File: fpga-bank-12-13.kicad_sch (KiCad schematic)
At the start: 5 parts, among them U1 XC7K410T-2FFG900I

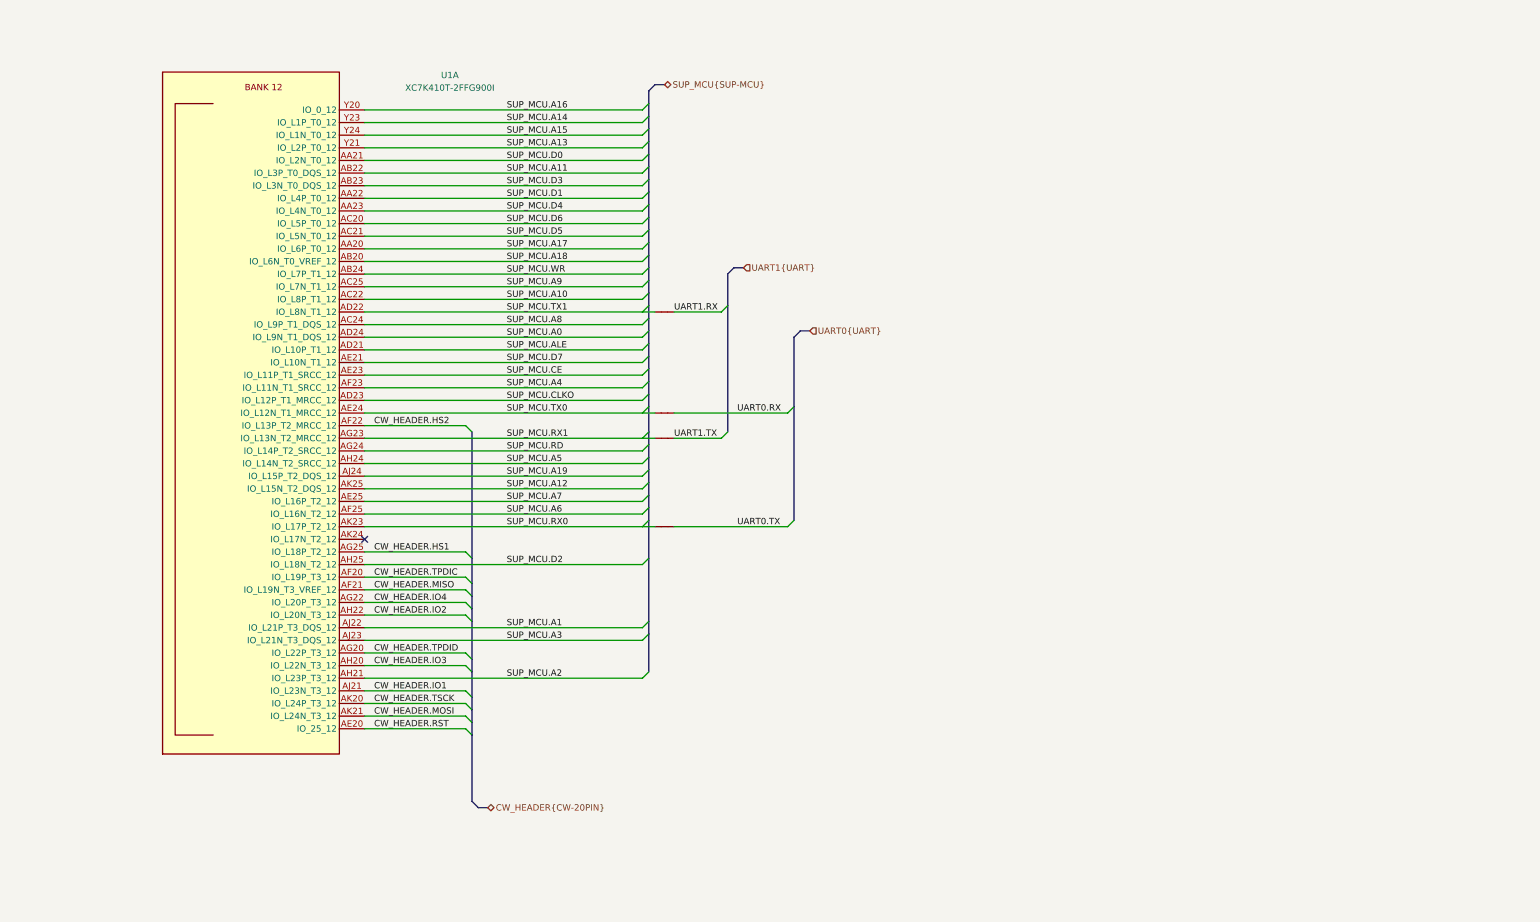
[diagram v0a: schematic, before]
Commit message: [#55729] Switch FPGA symbol to antmicroFPGAChips lib
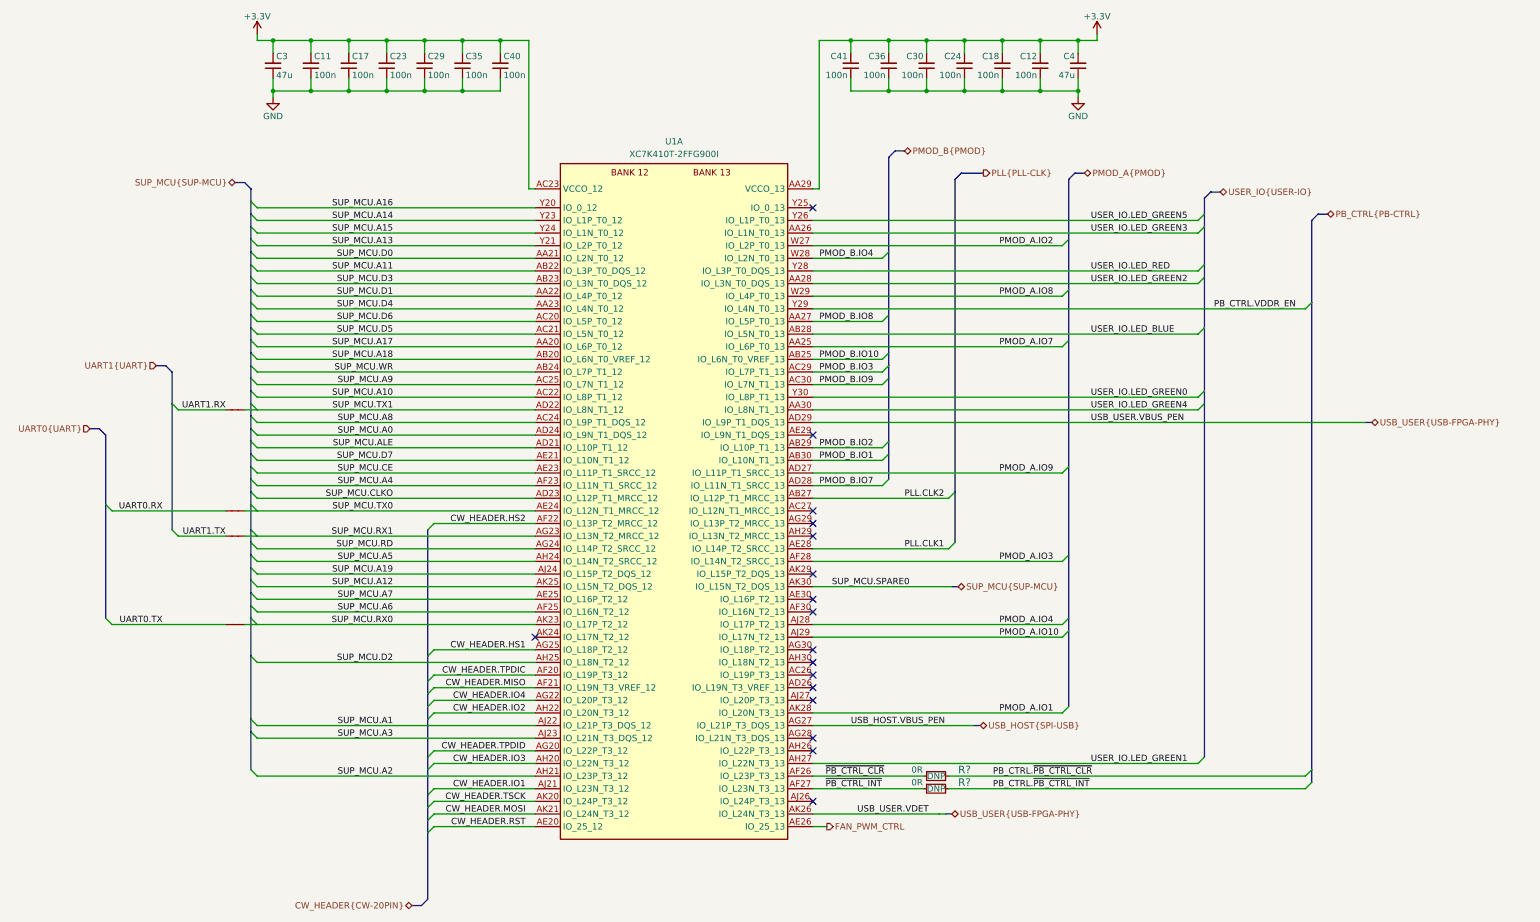
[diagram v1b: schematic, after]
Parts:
- added C11, C12, C17, C18, C23, C24, C29, C30, C35, C36, C40, C41: C_100n_0402, antmicro-footprints:C_0402_1005Metric, symbol antmicroCapacitors0402:C_100n_0402
- added C3, C4: C_47u_0603, antmicro-footprints:C_0603_1608Metric, symbol antmicroCapacitors0603:C_47u_0603
- added R? (x2): R_0R_0402, antmicro-footprints:R_0402_1005Metric, symbol antmicroResistors0402:R_0R_0402
- U1: footprint K410T-devboard-footprints:xc7k410t-2ffg900I -> antmicro-footprints:BGA-900_31x31mm_Layout30x30_P1x1mm_FFG900; symbol K410T-devboard:XC7K410T-2FFG900I -> antmicroFPGAChips:XC7K410T-2FFG900I
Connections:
- new net +3V3: C11.2, C12.2, C17.2, C18.2, C23.2, C24.2, C29.2, C3.2, C30.2, C35.2, C36.2, C4.2, C40.2, C41.2, U1.AA29 (VCCO_13), U1.AB26 (VCCO_13), U1.AC23 (VCCO_12), U1.AD20 (VCCO_12), U1.AD30 (VCCO_13), U1.AE27 (VCCO_13), U1.AF24 (VCCO_12), U1.AG21 (VCCO_12), U1.AH28 (VCCO_13), U1.AJ25 (VCCO_13), U1.AK22 (VCCO_12), U1.Y22 (VCCO_12)
- new net FAN_PWM_CTRL: U1.AE26 (IO_25_13)
- new net GND: C11.1, C12.1, C17.1, C18.1, C23.1, C24.1, C29.1, C3.1, C30.1, C35.1, C36.1, C4.1, C40.1, C41.1
- new net PB_CTRL.VDDR_EN: U1.Y29 (IO_L4N_T0_13)
- new net PB_CTRL.~{PB_CTRL_CLR}: R?.2
- new net PB_CTRL.~{PB_CTRL_INT}: R?.2
- new net PLL.CLK1: U1.AE28 (IO_L14P_T2_SRCC_13)
- new net PLL.CLK2: U1.AB27 (IO_L12P_T1_MRCC_13)
- new net PMOD_A.IO1: U1.AK28 (IO_L20N_T3_13)
- new net PMOD_A.IO10: U1.AJ29 (IO_L17N_T2_13)
- new net PMOD_A.IO2: U1.W27 (IO_L2P_T0_13)
- new net PMOD_A.IO3: U1.AF28 (IO_L14N_T2_SRCC_13)
- new net PMOD_A.IO4: U1.AJ28 (IO_L17P_T2_13)
- new net PMOD_A.IO7: U1.AA25 (IO_L6P_T0_13)
- new net PMOD_A.IO8: U1.W29 (IO_L4P_T0_13)
- new net PMOD_A.IO9: U1.AD27 (IO_L11P_T1_SRCC_13)
- new net PMOD_B.IO1: U1.AB30 (IO_L10N_T1_13)
- new net PMOD_B.IO10: U1.AB25 (IO_L6N_T0_VREF_13)
- new net PMOD_B.IO2: U1.AB29 (IO_L10P_T1_13)
- new net PMOD_B.IO3: U1.AC29 (IO_L7P_T1_13)
- new net PMOD_B.IO4: U1.W28 (IO_L2N_T0_13)
- new net PMOD_B.IO7: U1.AD28 (IO_L11N_T1_SRCC_13)
- new net PMOD_B.IO8: U1.AA27 (IO_L5P_T0_13)
- new net PMOD_B.IO9: U1.AC30 (IO_L7N_T1_13)
- new net SUP_MCU.SPARE0: U1.AK30 (IO_L15N_T2_DQS_13)
- new net USB_HOST.VBUS_PEN: U1.AG27 (IO_L21P_T3_DQS_13)
- new net USB_USER.VBUS_PEN: U1.AD29 (IO_L9P_T1_DQS_13)
- new net USB_USER.VDET: U1.AK26 (IO_L24N_T3_13)
- new net USER_IO.LED_BLUE: U1.AB28 (IO_L5N_T0_13)
- new net USER_IO.LED_GREEN0: U1.Y30 (IO_L8P_T1_13)
- new net USER_IO.LED_GREEN1: U1.AH27 (IO_L22N_T3_13)
- new net USER_IO.LED_GREEN2: U1.AA28 (IO_L3N_T0_DQS_13)
- new net USER_IO.LED_GREEN3: U1.AA26 (IO_L1N_T0_13)
- new net USER_IO.LED_GREEN4: U1.AA30 (IO_L8N_T1_13)
- new net USER_IO.LED_GREEN5: U1.Y26 (IO_L1P_T0_13)
- new net USER_IO.LED_RED: U1.Y28 (IO_L3P_T0_DQS_13)
- new net ~{PB_CTRL_CLR}: R?.1, U1.AF26 (IO_L23P_T3_13)
- new net ~{PB_CTRL_INT}: R?.1, U1.AF27 (IO_L23N_T3_13)
- no-connect marks 1 -> 17

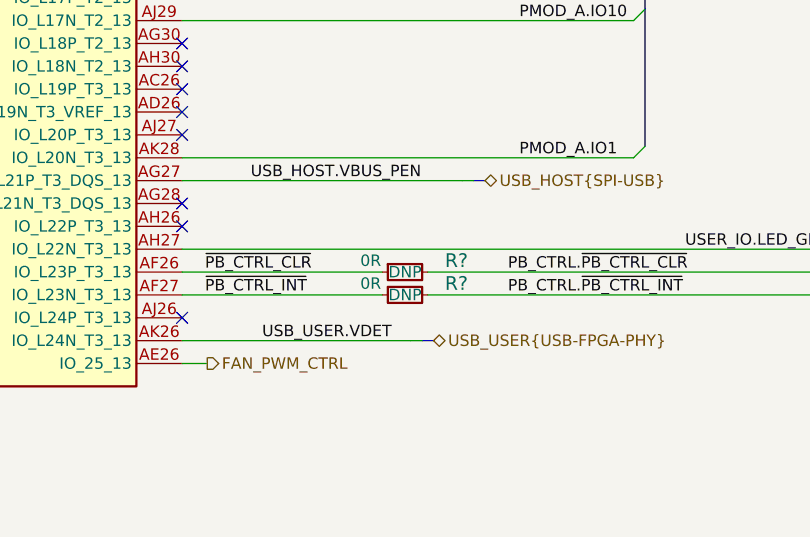
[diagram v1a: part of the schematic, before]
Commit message: [#55729] Globlib; Clean DNP; Realign to grid
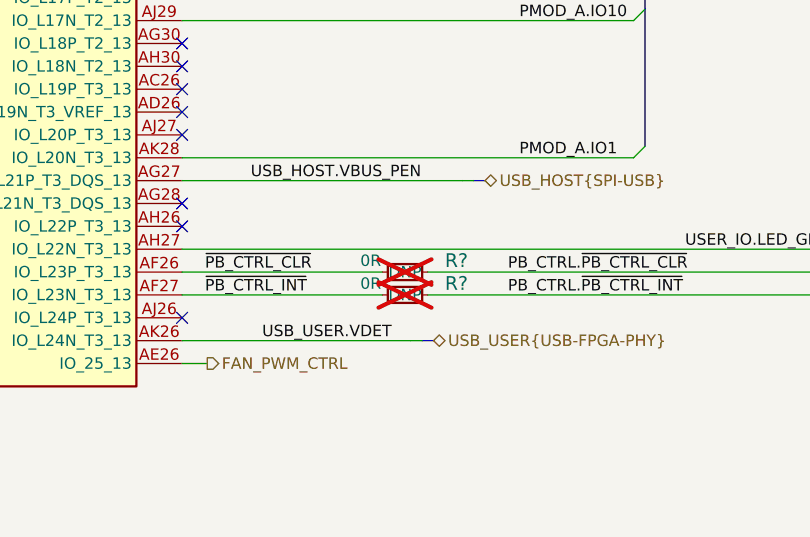
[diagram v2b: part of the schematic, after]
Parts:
- R? (x2): now not fitted; now left out of the parts list
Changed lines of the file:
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@@
   )
   (symbol (lib_id "antmicroResistors0402:R_0R_0402") (at 255.905 217.805 0) (unit 1)
-    (in_bom yes) (on_board yes) (dnp no)
+    (in_bom no) (on_board yes) (dnp yes)
     (property "Reference" "R?" (at 264.16 216.535 0)
       (effects (font (size 1.524 1.524)))
@@
   )
   (symbol (lib_id "antmicroResistors0402:R_0R_0402") (at 255.905 220.345 0) (unit 1)
-    (in_bom yes) (on_board yes) (dnp no)
+    (in_bom no) (on_board yes) (dnp yes)
     (property "Reference" "R?" (at 264.16 219.075 0)
       (effects (font (size 1.524 1.524)))

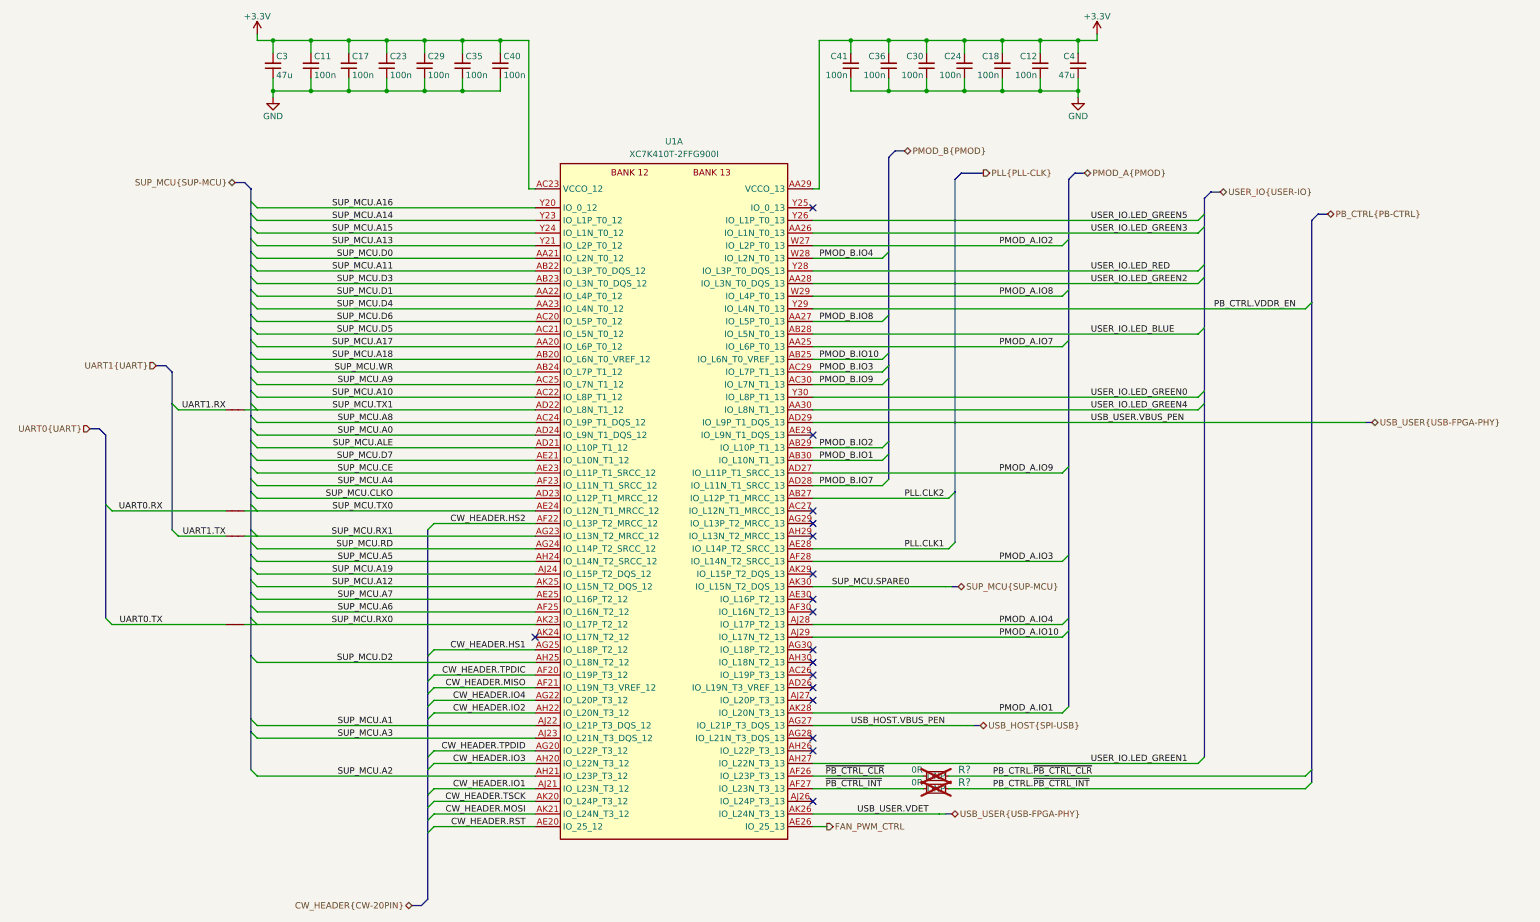
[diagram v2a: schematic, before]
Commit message: [#55729] Clean schematics/update from lib
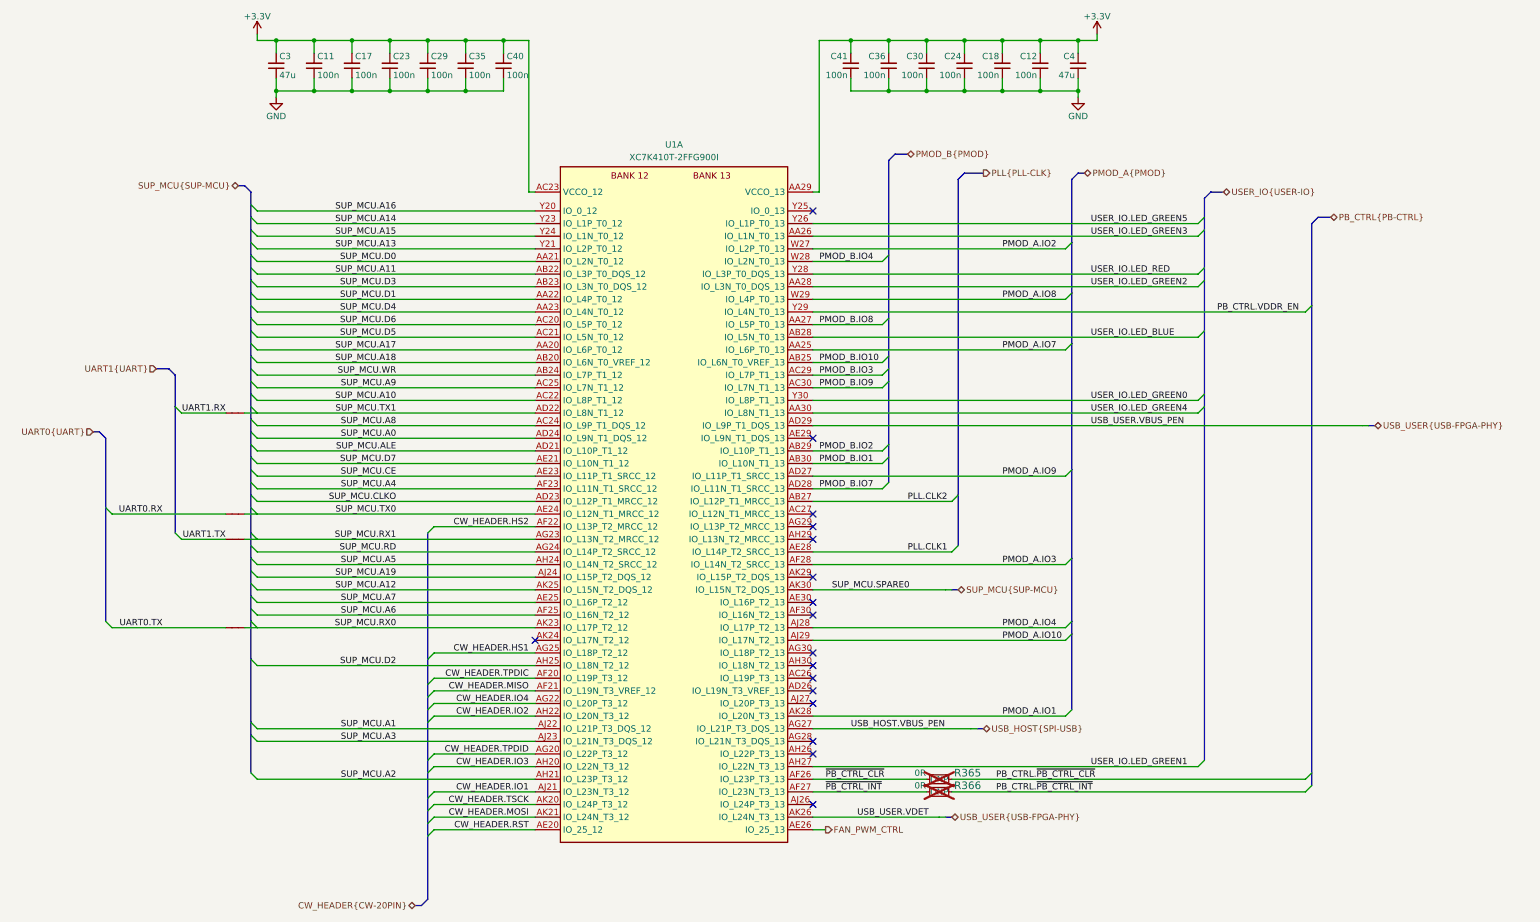
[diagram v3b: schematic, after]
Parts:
- gave numbers to parts that had none: 2
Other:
- moved on the sheet: C11, C17, C23, C29, C3, C35, C40, R365, R366, U1A

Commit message: [#55729] Update PCB from sch; Update fp from lib; Clean DRC
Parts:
- NT15, NT16, NT17, NT18: footprint K410T-devboard-footprints:NetTie-2_SMD_Pad0.127mm -> antmicro-footprints:NetTie-2_SMD_Pad0.127mm
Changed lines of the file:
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@@
       (effects (font (size 1.27 1.27) (thickness 0.15)) (justify left bottom) hide)
     )
-    (property "Footprint" "K410T-devboard-footprints:NetTie-2_SMD_Pad0.127mm" (at 97.79 170.18 0)
+    (property "Footprint" "antmicro-footprints:NetTie-2_SMD_Pad0.127mm" (at 97.79 170.18 0)
       (effects (font (size 1.27 1.27) (thickness 0.15)) (justify left bottom) hide)
     )
@@
       (effects (font (size 1.27 1.27) (thickness 0.15)) (justify left bottom) hide)
     )
-    (property "Footprint" "K410T-devboard-footprints:NetTie-2_SMD_Pad0.127mm" (at 97.79 193.04 0)
+    (property "Footprint" "antmicro-footprints:NetTie-2_SMD_Pad0.127mm" (at 97.79 193.04 0)
       (effects (font (size 1.27 1.27) (thickness 0.15)) (justify left bottom) hide)
     )
@@
       (effects (font (size 1.27 1.27) (thickness 0.15)) (justify left bottom) hide)
     )
-    (property "Footprint" "K410T-devboard-footprints:NetTie-2_SMD_Pad0.127mm" (at 97.79 175.26 0)
+    (property "Footprint" "antmicro-footprints:NetTie-2_SMD_Pad0.127mm" (at 97.79 175.26 0)
       (effects (font (size 1.27 1.27) (thickness 0.15)) (justify left bottom) hide)
     )
@@
       (effects (font (size 1.27 1.27) (thickness 0.15)) (justify left bottom) hide)
     )
-    (property "Footprint" "K410T-devboard-footprints:NetTie-2_SMD_Pad0.127mm" (at 97.79 149.86 0)
-      (effects (font (size 1.27 1.27) (thickness 0.15)) (justify left bottom) hide)
-    )
+    (property "Footprint" "antmicro-footprints:NetTie-2_SMD_Pad0.127mm" (at 97.79 149.86 0)
+      (effects (font (size 1.27 1.27) (thickness 0.15)) (justify left bottom) hide)
+    )
